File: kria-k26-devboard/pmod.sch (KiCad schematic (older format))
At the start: 7 parts, among them J4 SSW-106-02-G-D-RA, U14 TPD4E05U06QDQARQ1_PASS, U15 TPD4E05U06QDQARQ1_PASS

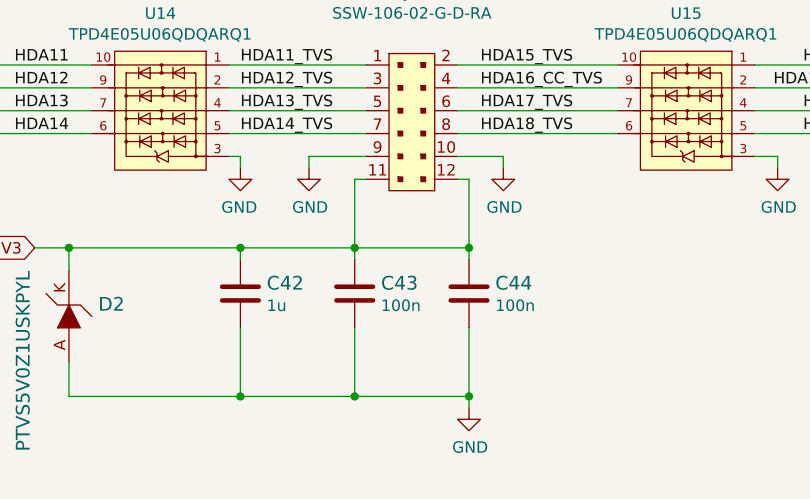
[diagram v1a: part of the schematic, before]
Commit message: Replaced 4A DC-DC conventer, finished cleaning after replacement
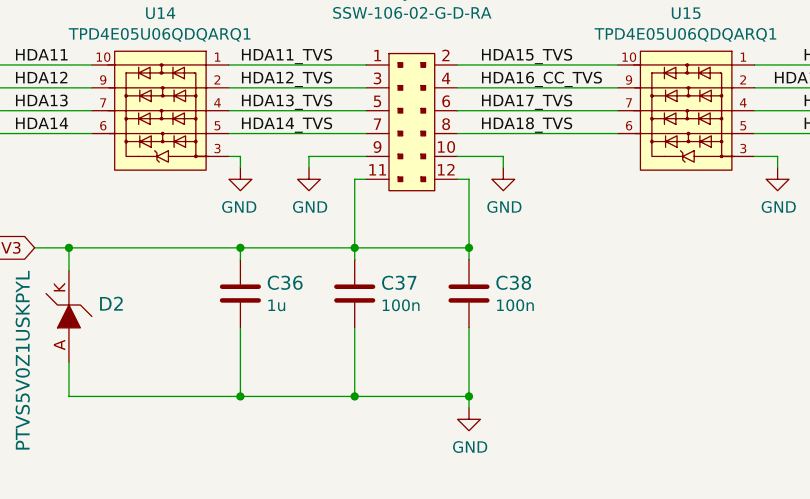
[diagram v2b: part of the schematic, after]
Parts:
- renumbered C42 to C36, C43 to C37, C44 to C38
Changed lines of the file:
@@
 	5150 3450 5150 3500
 $Comp
-L power:GND #PWR069
+L power:GND #PWR065
 U 1 1 649A6F75
 P 5150 3500
-F 0 "#PWR069" H 5150 3250 50  0001 C CNN
+F 0 "#PWR065" H 5150 3250 50  0001 C CNN
 F 1 "GND" H 5155 3327 50  0000 C CNN
 F 2 "" H 5150 3500 50  0001 C CNN
@@
 $EndComp
 $Comp
-L power:GND #PWR071
+L power:GND #PWR067
 U 1 1 649A7323
 P 6000 3500
-F 0 "#PWR071" H 6000 3250 50  0001 C CNN
+F 0 "#PWR067" H 6000 3250 50  0001 C CNN
 F 1 "GND" H 6005 3327 50  0000 C CNN
 F 2 "" H 6000 3500 50  0001 C CNN
@@
 PL_3V3
 $Comp
-L antmicroCapacitors0402:C_100n_0402 C43
+L antmicroCapacitors0402:C_100n_0402 C37
 U 1 1 649C2025
 P 5350 4050
-F 0 "C43" H 5465 4095 60  0000 L CNN
+F 0 "C37" H 5465 4095 60  0000 L CNN
 F 1 "C_100n_0402" H 5350 3900 60  0001 C CNN
 F 2 "antmicro-footprints:0402-cap" H 5550 4250 60  0001 L CNN
@@
 $EndComp
 $Comp
-L antmicroCapacitors0402:C_100n_0402 C44
+L antmicroCapacitors0402:C_100n_0402 C38
 U 1 1 649C25C6
 P 5850 4050
-F 0 "C44" H 5965 4095 60  0000 L CNN
+F 0 "C38" H 5965 4095 60  0000 L CNN
 F 1 "C_100n_0402" H 5850 3900 60  0001 C CNN
 F 2 "antmicro-footprints:0402-cap" H 6050 4250 60  0001 L CNN
@@
 $EndComp
 $Comp
-L antmicroCapacitors0402:C_1u_0402 C42
+L antmicroCapacitors0402:C_1u_0402 C36
 U 1 1 649C4ADC
 P 4850 4050
-F 0 "C42" H 4965 4095 60  0000 L CNN
+F 0 "C36" H 4965 4095 60  0000 L CNN
 F 1 "C_1u_0402" H 4850 3900 60  0001 C CNN
 F 2 "antmicro-footprints:0402-cap" H 5050 4250 60  0001 L CNN
@@
 Connection ~ 4850 3850
 $Comp
-L power:GND #PWR070
+L power:GND #PWR066
 U 1 1 649DA63B
 P 5850 4550
-F 0 "#PWR070" H 5850 4300 50  0001 C CNN
+F 0 "#PWR066" H 5850 4300 50  0001 C CNN
 F 1 "GND" H 5855 4377 50  0000 C CNN
 F 2 "" H 5850 4550 50  0001 C CNN
@@
 	4850 3450 4850 3500
 $Comp
-L power:GND #PWR0406
+L power:GND #PWR064
 U 1 1 68DC2BFC
 P 4850 3500
-F 0 "#PWR0406" H 4850 3250 50  0001 C CNN
+F 0 "#PWR064" H 4850 3250 50  0001 C CNN
 F 1 "GND" H 4855 3327 50  0000 C CNN
 F 2 "" H 4850 3500 50  0001 C CNN
@@
 	7200 3450 7200 3500
 $Comp
-L power:GND #PWR0407
+L power:GND #PWR068
 U 1 1 68E4E367
 P 7200 3500
-F 0 "#PWR0407" H 7200 3250 50  0001 C CNN
+F 0 "#PWR068" H 7200 3250 50  0001 C CNN
 F 1 "GND" H 7205 3327 50  0000 C CNN
 F 2 "" H 7200 3500 50  0001 C CNN

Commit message: Locklib+ added layer table
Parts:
- C36: footprint antmicro-footprints:0402-cap -> kria-k26-devboard-footprints:0402-cap; symbol antmicroCapacitors0402:C_1u_0402 -> kria-k26-devboard:C_1u_0402
- C37, C38: footprint antmicro-footprints:0402-cap -> kria-k26-devboard-footprints:0402-cap; symbol antmicroCapacitors0402:C_100n_0402 -> kria-k26-devboard:C_100n_0402
- D2: footprint antmicro-footprints:SOD-964 -> kria-k26-devboard-footprints:SOD-964; symbol antmicroTVSDiodes:PTVS5V0Z1USKPYL -> kria-k26-devboard:PTVS5V0Z1USKPYL
- J4: footprint antmicro-footprints:SAMTEC_SSW-106-02-G-D-RA -> kria-k26-devboard-footprints:SAMTEC_SSW-106-02-G-D-RA; symbol antmicroRectangularConnectorsHeadersFemalePins:SSW-106-02-G-D-RA -> kria-k26-devboard:SSW-106-02-G-D-RA
- U14, U15: footprint antmicro-footprints:TPD4E05U06QDQARQ1 -> kria-k26-devboard-footprints:TPD4E05U06QDQARQ1; symbol antmicroTVSDiodes:TPD4E05U06QDQARQ1_PASS -> kria-k26-devboard:TPD4E05U06QDQARQ1_PASS
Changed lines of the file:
@@
 $EndDescr
 $Comp
-L antmicroRectangularConnectorsHeadersFemalePins:SSW-106-02-G-D-RA J4
+L kria-k26-devboard:SSW-106-02-G-D-RA J4
 U 1 1 649925B1
 P 5600 3300
 F 0 "J4" H 5600 3867 50  0000 C CNN
 F 1 "SSW-106-02-G-D-RA" H 5600 3776 50  0000 C CNN
-F 2 "antmicro-footprints:SAMTEC_SSW-106-02-G-D-RA" H 5200 3850 50  0001 L BNN
+F 2 "kria-k26-devboard-footprints:SAMTEC_SSW-106-02-G-D-RA" H 5200 3850 50  0001 L BNN
 F 3 "https://suddendocs.samtec.com/prints/ssw-1xx-xx-xxx-x-xx-xxx-xx-mkt.pdf" H 5600 3300 50  0001 L BNN
 F 4 "Samtec Inc." H 5300 3950 50  0001 L BNN "Manufacturer"
@@
 	5150 3450 5150 3500
 $Comp
-L power:GND #PWR065
+L kria-k26-devboard:GND #PWR065
 U 1 1 649A6F75
 P 5150 3500
@@
 $EndComp
 $Comp
-L power:GND #PWR067
+L kria-k26-devboard:GND #PWR067
 U 1 1 649A7323
 P 6000 3500
@@
 PL_3V3
 $Comp
-L antmicroCapacitors0402:C_100n_0402 C37
+L kria-k26-devboard:C_100n_0402 C37
 U 1 1 649C2025
 P 5350 4050
 F 0 "C37" H 5465 4095 60  0000 L CNN
 F 1 "C_100n_0402" H 5350 3900 60  0001 C CNN
-F 2 "antmicro-footprints:0402-cap" H 5550 4250 60  0001 L CNN
+F 2 "kria-k26-devboard-footprints:0402-cap" H 5550 4250 60  0001 L CNN
 F 3 "" H 5350 4050 50  0001 C CNN
 F 4 "Murata" H 5550 4450 60  0001 L CNN "Manufacturer"
@@
 $EndComp
 $Comp
-L antmicroCapacitors0402:C_100n_0402 C38
+L kria-k26-devboard:C_100n_0402 C38
 U 1 1 649C25C6
 P 5850 4050
 F 0 "C38" H 5965 4095 60  0000 L CNN
 F 1 "C_100n_0402" H 5850 3900 60  0001 C CNN
-F 2 "antmicro-footprints:0402-cap" H 6050 4250 60  0001 L CNN
+F 2 "kria-k26-devboard-footprints:0402-cap" H 6050 4250 60  0001 L CNN
 F 3 "" H 5850 4050 50  0001 C CNN
 F 4 "Murata" H 6050 4450 60  0001 L CNN "Manufacturer"
@@
 $EndComp
 $Comp
-L antmicroCapacitors0402:C_1u_0402 C36
+L kria-k26-devboard:C_1u_0402 C36
 U 1 1 649C4ADC
 P 4850 4050
 F 0 "C36" H 4965 4095 60  0000 L CNN
 F 1 "C_1u_0402" H 4850 3900 60  0001 C CNN
-F 2 "antmicro-footprints:0402-cap" H 5050 4250 60  0001 L CNN
+F 2 "kria-k26-devboard-footprints:0402-cap" H 5050 4250 60  0001 L CNN
 F 3 "" H 4850 4050 50  0001 C CNN
 F 4 "TDK" H 5050 4450 60  0001 L CNN "Manufacturer"
@@
 Connection ~ 4850 3850
 $Comp
-L power:GND #PWR066
+L kria-k26-devboard:GND #PWR066
 U 1 1 649DA63B
 P 5850 4550
@@
 Connection ~ 4850 4500
 $Comp
-L antmicroTVSDiodes:PTVS5V0Z1USKPYL D2
+L kria-k26-devboard:PTVS5V0Z1USKPYL D2
 U 1 1 69B7F430
 P 4100 4150
 F 0 "D2" V 4153 4022 60  0000 R CNN
 F 1 "PTVS5V0Z1USKPYL" H 4300 4350 60  0000 R CNN
-F 2 "antmicro-footprints:SOD-964" H 4300 4350 60  0001 L CNN
+F 2 "kria-k26-devboard-footprints:SOD-964" H 4300 4350 60  0001 L CNN
 F 3 "https://pl.mouser.com/datasheet/2/916/PTVS5V0Z1USKP-1600477.pdf" H 4300 4450 60  0001 L CNN
 F 4 "Nexperia" H 4300 5250 60  0001 L CNN "Manufacturer"
@@
 	4100 4350 4100 4500
 $Comp
-L antmicroTVSDiodes:TPD4E05U06QDQARQ1_PASS U14
+L kria-k26-devboard:TPD4E05U06QDQARQ1_PASS U14
 U 1 1 68DA8E80
 P 4750 3250
 F 0 "U14" H 5000 3675 50  0000 C CNN
 F 1 "TPD4E05U06QDQARQ1_PASS" H 4550 2900 50  0001 L CNN
-F 2 "antmicro-footprints:TPD4E05U06QDQARQ1" H 4800 3700 50  0001 L CNN
+F 2 "kria-k26-devboard-footprints:TPD4E05U06QDQARQ1" H 4800 3700 50  0001 L CNN
 F 3 "https://www.ti.com/lit/ds/symlink/tpd4e05u06-q1.pdf?ts=1652104096549" H 4750 3650 50  0001 L CNN
 F 4 "Texas Instruments" H 5100 3900 50  0001 C CNN "Manufacturer"
@@
 	4850 3450 4850 3500
 $Comp
-L power:GND #PWR064
+L kria-k26-devboard:GND #PWR064
 U 1 1 68DC2BFC
 P 4850 3500
@@
 	4800 3350 5400 3350
 $Comp
-L antmicroTVSDiodes:TPD4E05U06QDQARQ1_PASS U15
+L kria-k26-devboard:TPD4E05U06QDQARQ1_PASS U15
 U 1 1 68DF9EF9
 P 7050 3250
 F 0 "U15" H 7300 3675 50  0000 C CNN
 F 1 "TPD4E05U06QDQARQ1_PASS" H 6850 2900 50  0001 L CNN
-F 2 "antmicro-footprints:TPD4E05U06QDQARQ1" H 7100 3700 50  0001 L CNN
+F 2 "kria-k26-devboard-footprints:TPD4E05U06QDQARQ1" H 7100 3700 50  0001 L CNN
 F 3 "https://www.ti.com/lit/ds/symlink/tpd4e05u06-q1.pdf?ts=1652104096549" H 7050 3650 50  0001 L CNN
 F 4 "Texas Instruments" H 7400 3900 50  0001 C CNN "Manufacturer"
@@
 	7200 3450 7200 3500
 $Comp
-L power:GND #PWR068
+L kria-k26-devboard:GND #PWR068
 U 1 1 68E4E367
 P 7200 3500
